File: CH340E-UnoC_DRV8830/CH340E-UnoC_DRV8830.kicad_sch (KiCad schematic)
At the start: 4 parts, among them J1 Power, J2 Digital/PWM, J3 Analog, J4 Digital/PWM

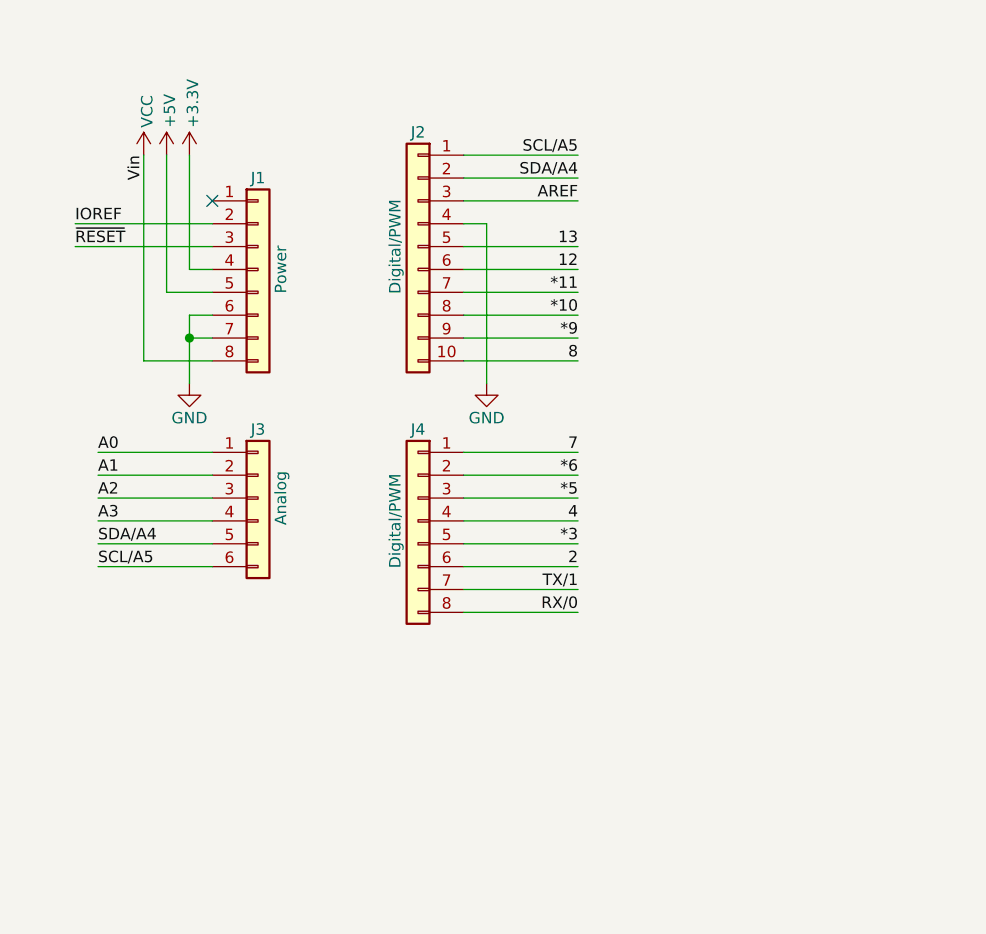
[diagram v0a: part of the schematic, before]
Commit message: feat: Atmega328P-PU was added to the schematic.
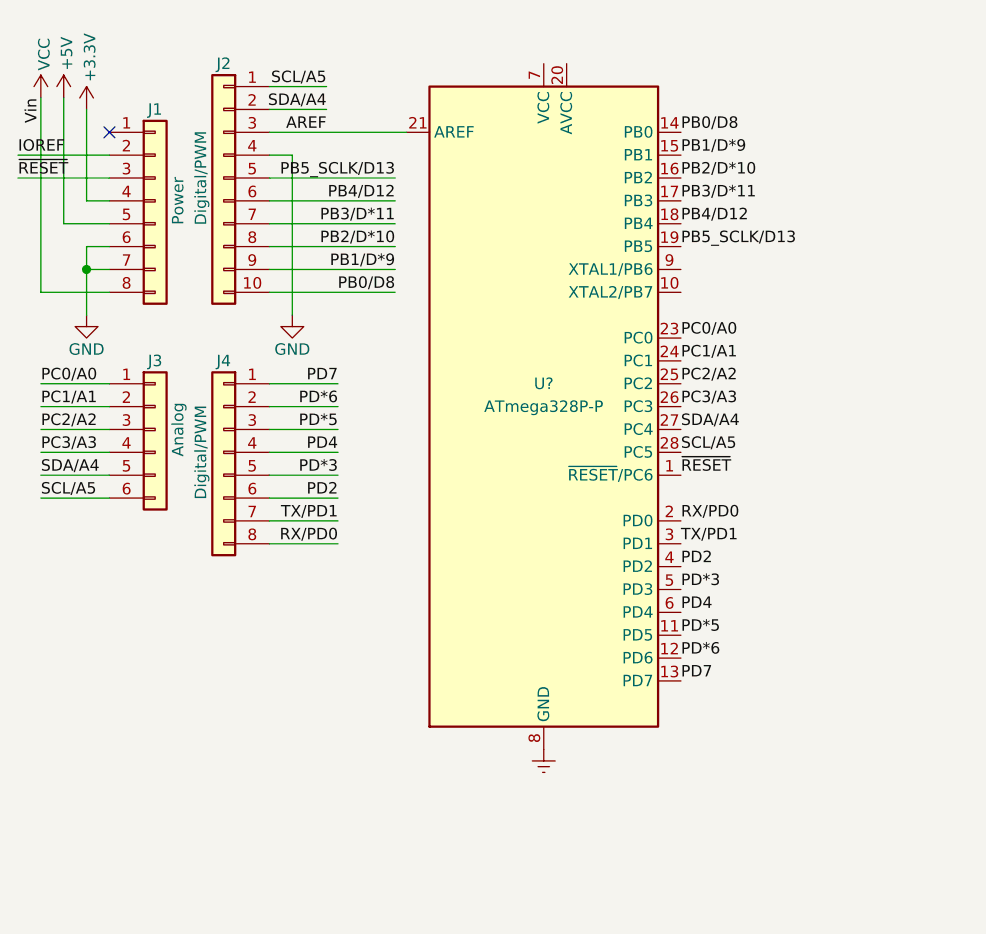
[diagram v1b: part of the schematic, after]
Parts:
- added U?: ATmega328P-P, Package_DIP:DIP-28_W7.62mm, symbol MCU_Microchip_ATmega:ATmega328P-P
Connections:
- net AREF: now also U?.21 (AREF)
- net SCL/A5: now also U?.28 (PC5)
- net SDA/A4: now also U?.27 (PC4)
- net ~{RESET}: now also U?.1 (~{RESET}/PC6)
- net *10 renamed PB2/D*10
- net PB2/D*10: now also U?.16 (PB2)
- net *11 renamed PB3/D*11
- net PB3/D*11: now also U?.17 (PB3)
- net *3 renamed PD*3
- net PD*3: now also U?.5 (PD3)
- net *5 renamed PD*5
- net PD*5: now also U?.11 (PD5)
- net *6 renamed PD*6
- net PD*6: now also U?.12 (PD6)
- net *9 renamed PB1/D*9
- net PB1/D*9: now also U?.15 (PB1)
- net 12 renamed PB4/D12
- net PB4/D12: now also U?.18 (PB4)
- net 13 renamed PB5_SCLK/D13
- net PB5_SCLK/D13: now also U?.19 (PB5)
- net 2 renamed PD2
- net PD2: now also U?.4 (PD2)
- net 4 renamed PD4
- net PD4: now also U?.6 (PD4)
- net 7 renamed PD7
- net PD7: now also U?.13 (PD7)
- net 8 renamed PB0/D8
- net PB0/D8: now also U?.14 (PB0)
- net A0 renamed PC0/A0
- net PC0/A0: now also U?.23 (PC0)
- net A1 renamed PC1/A1
- net PC1/A1: now also U?.24 (PC1)
- net A2 renamed PC2/A2
- net PC2/A2: now also U?.25 (PC2)
- net A3 renamed PC3/A3
- net PC3/A3: now also U?.26 (PC3)
- net RX/0 renamed RX/PD0
- net RX/PD0: now also U?.2 (PD0)
- net TX/1 renamed TX/PD1
- net TX/PD1: now also U?.3 (PD1)
- new net Earth: U?.22 (GND), U?.8 (GND)
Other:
- moved on the sheet: J1, J2, J3, J4

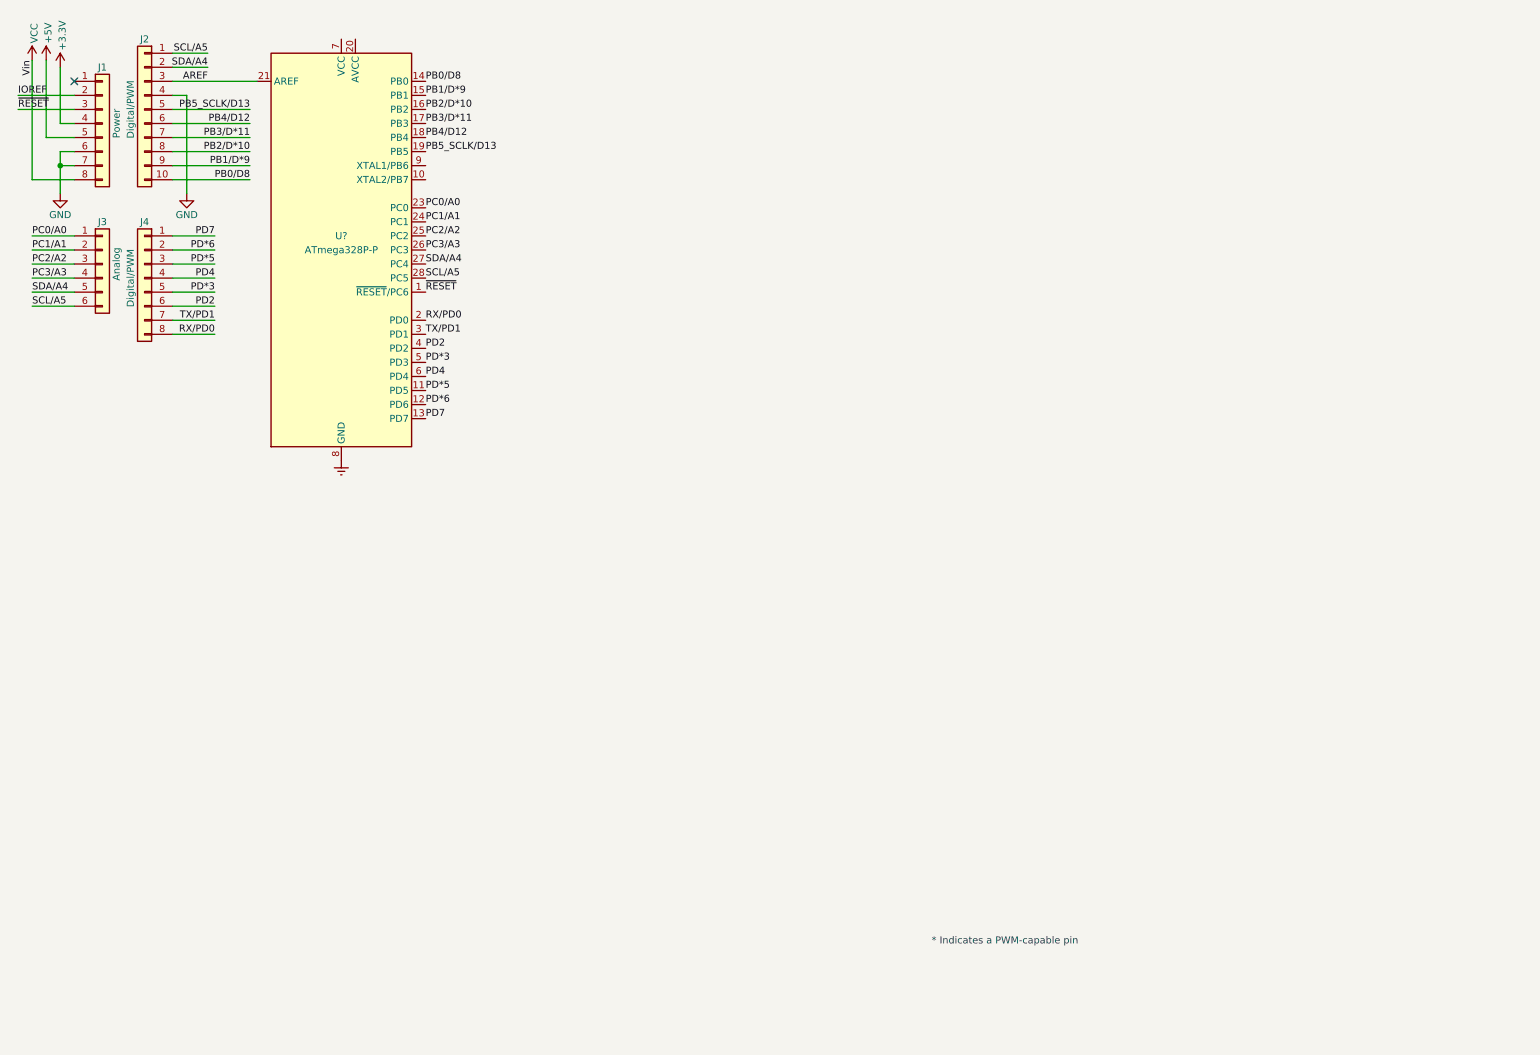
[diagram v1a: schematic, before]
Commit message: feat: Create Arduino Uno schematic using CH340E.
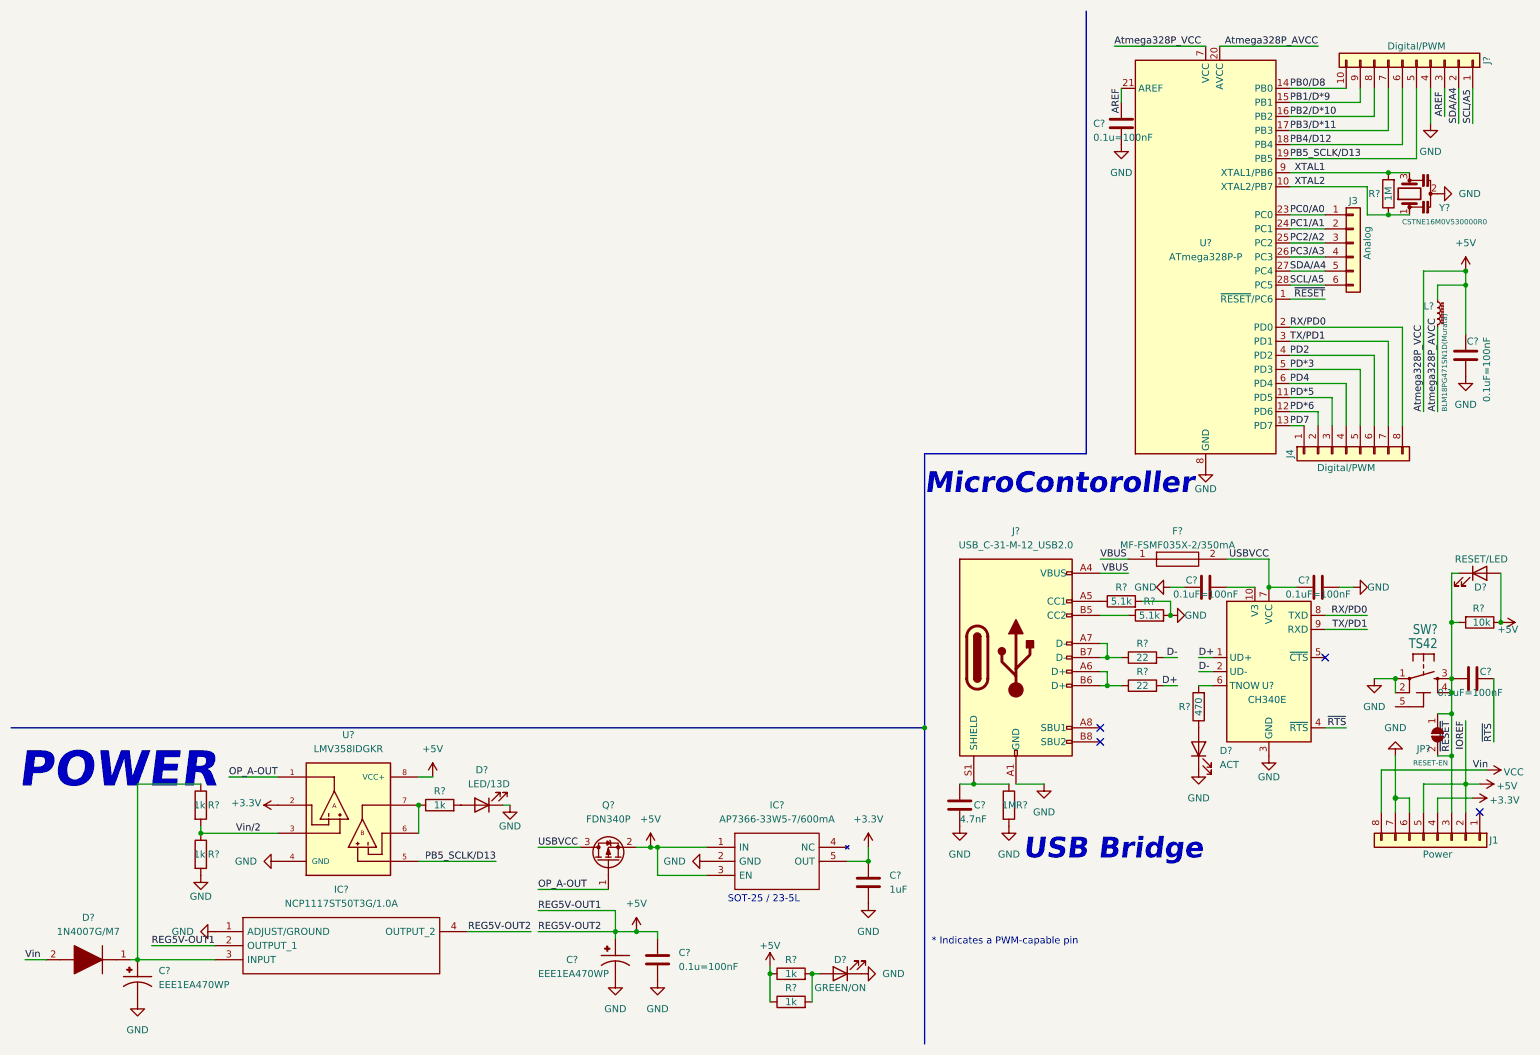
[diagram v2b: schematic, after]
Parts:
- removed J2: Digital/PWM, Connector_PinSocket_2.54mm:PinSocket_1x10_P2.54mm_Vertical, symbol Connector_Generic:Conn_01x10
- added C?: 1uF, symbol Device:C
- added C? (x2): 0.1u=100nF, symbol Device:C
- added C?: 4.7nF, symbol Device:C
- added C? (x2): EEE1EA470WP, CAP_EEE1EA470WP, symbol Capacitors-EEE1EA470WP_SnapEDA:EEE1EA470WP
- added C? (x4): 0.1uF=100nF, symbol Device:C
- added D?: ACT, symbol Device:LED
- added D?: GREEN/ON, symbol Device:LED
- added D?: RESET/LED, symbol Device:LED
- added D?: LED/13D, symbol Device:LED
- added D?: 1N4007G/M7, DIOM5025X220N, symbol Diode-1N4007G_SamacSys:1N4007G
- added F?: MF-FSMF035X-2/350mA, FUSC1608X65N, symbol Fuse_MF-FSMF035X-2_SamacSys:MF-FSMF035X-2
- added IC?: NCP1117ST50T3G/1.0A, SOT230P700X180-4N, symbol IC-Reg_NCP1117ST50T3G_SamacSys:NCP1117ST50T3G
- added IC?: AP7366-33W5-7/600mA, SOT95P285X130-5N, symbol IC-Reg_AP7366-33W5-7_SamacSys:AP7366-33W5-7
- added J?: Digital/PWM, Connector_PinSocket_2.54mm:PinSocket_1x10_P2.54mm_Vertical, symbol Connector_Generic:Conn_01x10
- added J?: USB_C-31-M-12_USB2.0, symbol Connector:USB_C_Receptacle_USB2.0
- added JP?: RESET-EN, symbol Jumper:SolderJumper_2_Open
- added L?: BLM18PG471SN1D(Murata), symbol Device:L_Ferrite_Small
- added Q?: FDN340P, Package_TO_SOT_SMD:SOT-23, symbol Transistor_FET:FDN340P
- added R?: 10k, symbol Device:R
- added R? (x2): 22, symbol Device:R
- added R? (x5): 1k, symbol Device:R
- added R?: 470, symbol Device:R
- added R? (x2): 1M, symbol Device:R
- added R? (x2): 5.1k, symbol Device:R
- added SW?: TS42, UNO-TH_Rev3e:TS42, symbol UNO-TH_Rev3e-eagle-import:TS42
- added U?: CH340E, Package_SO:MSOP-10_3x3mm_P0.5mm, symbol Interface_USB:CH340E
- added U?: LMV358IDGKR, SOP65P490X110-8N, symbol OPAmpDual_LMV358IDGKR_SnapEDA:LMV358IDGKR
- added Y?: CSTNE16M0V530000R0, symbol Device:Resonator
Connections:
- net Earth is gone; now on net GND: U?.22 (GND), U?.8 (GND)
- net IOREF is gone; now on net +5V: J1.2 (Pin_2)
- net +3V3: now also U?.2
- net +5V: now also U?.7 (VCC), C?.1, C?.1, C?.2, D?.2 (A), IC?.1 (IN), IC?.2 (OUTPUT_1), IC?.3 (EN), IC?.4 (OUTPUT_2), L?.1, Q?.2 (S), R?.1, R?.1, R?.1, U?.8 (VCC+)
- net AREF: now also C?.1, J?.3 (Pin_3)
- net GND: now also C?.1, C?.1, C?.2, C?.2, C?.2, C?.2, C?.2, C?.2, C?.2, D?.1 (K), D?.1 (K), D?.1 (K), IC?.1 (ADJUST/GROUND), IC?.2 (GND), J?.4 (Pin_4), J?.A1 (GND), J?.A12 (GND), J?.B1 (GND), J?.B12 (GND), R?.2, R?.2, R?.2, R?.2, SW?.1, SW?.2, U?.3 (GND), U?.4 (GND), Y?.2
- net PB0/D8: now also J?.10 (Pin_10)
- net PB1/D*9: now also J?.9 (Pin_9)
- net PB2/D*10: now also J?.8 (Pin_8)
- net PB3/D*11: now also J?.7 (Pin_7)
- net PB4/D12: now also J?.6 (Pin_6)
- net PB5_SCLK/D13: now also J?.5 (Pin_5), U?.5
- net RX/PD0: now also U?.8 (TXD)
- net SCL/A5: now also J?.1 (Pin_1)
- net SDA/A4: now also J?.2 (Pin_2)
- net TX/PD1: now also U?.9 (RXD)
- net VCC: now also D?.2
- net ~{RESET}: now also C?.2, D?.1 (K), JP?.1 (A), JP?.2 (B), R?.2, SW?.3, SW?.4
- net XTAL2: now reaches U?.10 (XTAL2/PB7)
- net XTAL2: now also R?.1, Y?.1
- net Atmega328P_AVCC: now reaches U?.20 (AVCC)
- net Atmega328P_AVCC: now also L?.2
- net XTAL1: now reaches U?.9 (XTAL1/PB6)
- net XTAL1: now also R?.2, Y?.3
- new net: C?.1, D?.1, IC?.3 (INPUT), R?.1
- new net: D?.2 (A), R?.1
- new net: D?.2 (A), R?.2, R?.2
- new net: C?.2, U?.10 (V3)
- new net: R?.2, U?.6 (TNOW)
- new net: J?.A6 (D+), J?.B6 (D+), R?.1
- new net: R?.1, U?.6, U?.7
- new net: D?.2 (A), R?.2
- new net: C?.1, J?.S1 (SHIELD), R?.1
- new net: J?.A7 (D-), J?.B7 (D-), R?.1
- new net: J?.A5 (CC1), R?.1
- new net: J?.B5 (CC2), R?.1
- new net +3.3V: C?.1, IC?.5 (OUT)
- new net D+: R?.2, U?.1 (UD+)
- new net D-: R?.2, U?.2 (UD-)
- new net OP_A-OUT: Q?.1 (G), U?.1
- new net USBVCC: C?.1, F?.2, Q?.3 (D), U?.7 (VCC)
- new net VBUS: F?.1, J?.A4 (VBUS), J?.A9 (VBUS), J?.B4 (VBUS), J?.B9 (VBUS)
- new net Vin/2: R?.1, R?.2, U?.3
- new net ~{RTS}: C?.1, U?.4 (~{RTS})
- no-connect marks 1 -> 4
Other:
- note added: "MicroContoroller"
- note added: "POWER"
- note added: "SOT-25 / 23-5L"
- note added: "USB Bridge"
- moved on the sheet: J1, J3, J4, U?

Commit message: feat: I have created a schematic of a motor driver using the DRV8830IC. A library of components has been added accordingly.
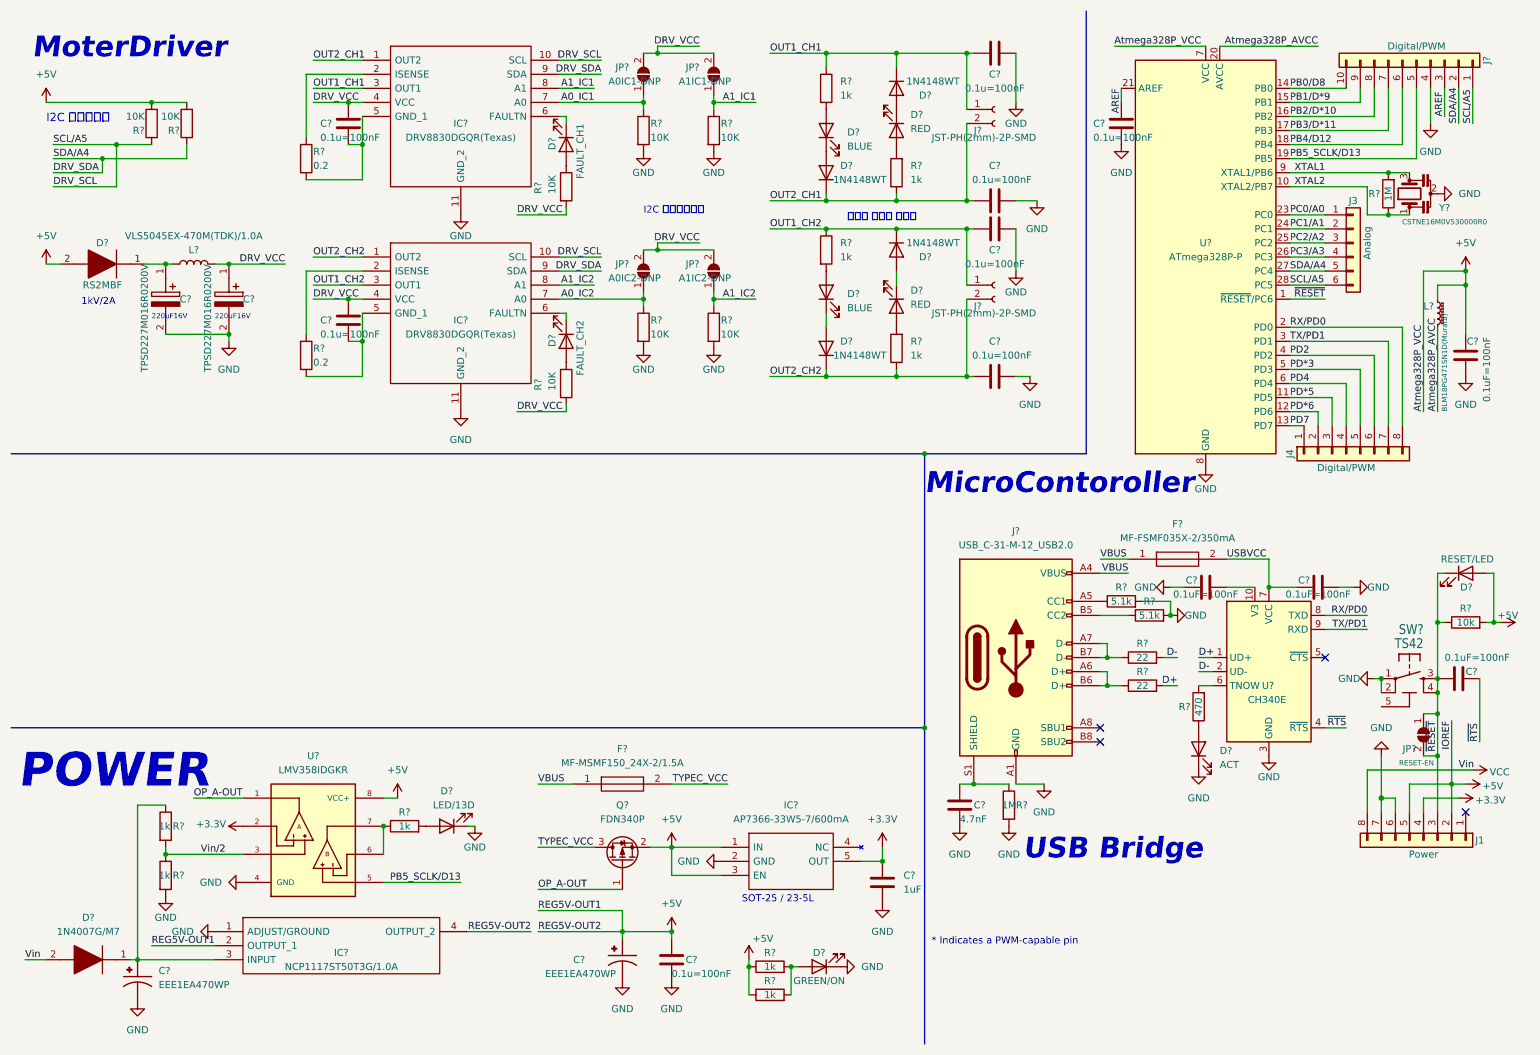
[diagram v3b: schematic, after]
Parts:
- removed R?: 10k, symbol Device:R
- added C? (x2): TPSD227M016R0200V, CAPPM7344X310N, symbol Cap220uF16V_TPSD227M016R0200V_SamacSys:TPSD227M016R0200V
- added C? (x6): 0.1u=100nF, Capacitor_SMD:C_0402_1005Metric, symbol Device:C
- added D? (x4): 1N4148WT, Diode_SMD:D_SOD-523, symbol Diode:1N4148WT
- added D? (x2): BLUE, LED_SMD:LED_0402_1005Metric, symbol Device:LED
- added D?: FAULT_CH2, LED_SMD:LED_0402_1005Metric, symbol Device:LED
- added D? (x2): RED, LED_SMD:LED_0402_1005Metric, symbol Device:LED
- added D?: RS2MBF, SODFL5336X130N, symbol Diodes1kV2A_RS2MBF_SMD_SamacSys:RS2MBF
- added D?: FAULT_CH1, LED_SMD:LED_0402_1005Metric, symbol Device:LED
- added F?: MF-MSMF150_24X-2/1.5A, FUSC4632X160N, symbol Fuse_MF-MSMF150_24X-2_1812 (4532 Metric)_SamacSys:MF-MSMF150_24X-2
- added IC? (x2): DRV8830DGQR(Texas), SOP50P490X110-11N, symbol IC-DRV8830DGQR_SamacSys:DRV8830DGQR
- added J? (x2): JST-PH(2mm)-2P-SMD, Connector_JST:JST_PH_B2B-PH-SM4-TB_1x02-1MP_P2.00mm_Vertical, symbol Connector:Conn_01x02_Female
- added JP?: A1IC2-DNP, symbol Jumper:SolderJumper_2_Open
- added JP?: A0IC1-DNP, symbol Jumper:SolderJumper_2_Open
- added JP?: A0IC2-DNP, symbol Jumper:SolderJumper_2_Open
- added JP?: A1IC1-DNP, symbol Jumper:SolderJumper_2_Open
- added L?: VLS5045EX-470M(TDK)/1.0A, symbol Device:L
- added R? (x4): 1k, Resistor_SMD:R_0402_1005Metric, symbol Device:R
- added R? (x8): 10K, Resistor_SMD:R_0402_1005Metric, symbol Device:R
- added R?: 10k, symbol Device:R
- added R? (x2): 0.2, Resistor_SMD:R_0402_1005Metric, symbol Device:R
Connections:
- net +5V: now also D?.2, R?.2, R?.2, R?.2
- net GND: now also C?.2, C?.2, C?.2, C?.2, C?.2, C?.2, IC?.11 (GND_2), IC?.11 (GND_2), R?.2, R?.2, R?.2, R?.2
- net USBVCC: no longer Q?.3 (D)
- net VBUS: now also F?.1
- net ~{RESET}: now also R?.1
- net SCL/A5 renamed DRV_SCL
- net DRV_SCL: now also IC?.10 (SCL), IC?.10 (SCL), R?.1
- net SDA/A4 renamed DRV_SDA
- net DRV_SDA: now also IC?.9 (SDA), IC?.9 (SDA), R?.1
- new net: D?.1 (K), D?.2 (A) (x4)
- new net: D?.2 (A), R?.2 (x4)
- new net: D?.2 (A), R?.1 (x2)
- new net: C?.1, D?.1, L?.1
- new net: IC?.2 (ISENSE), R?.1 (x2)
- new net: C?.2, IC?.5 (GND_1), R?.2 (x2)
- new net: D?.1 (K), IC?.6 (FAULTN) (x2)
- new net A0_IC1: IC?.7 (A0), JP?.1 (A), R?.1
- new net A0_IC2: IC?.7 (A0), JP?.1 (A), R?.1
- new net A1_IC1: IC?.8 (A1), JP?.1 (A), R?.1
- new net A1_IC2: IC?.8 (A1), JP?.1 (A), R?.1
- new net DRV_VCC: C?.1, C?.1, C?.1, IC?.4 (VCC), IC?.4 (VCC), JP?.2 (B), JP?.2 (B), JP?.2 (B), JP?.2 (B), L?.2, R?.2, R?.2
- new net OUT1_CH1: C?.1, D?.1 (K), IC?.3 (OUT1), J?.1 (Pin_1), R?.1
- new net OUT1_CH2: C?.1, D?.1 (K), IC?.3 (OUT1), J?.1 (Pin_1), R?.1
- new net OUT2_CH1: C?.1, D?.1 (K), IC?.1 (OUT2), J?.2 (Pin_2), R?.1
- new net OUT2_CH2: C?.1, D?.1 (K), IC?.1 (OUT2), J?.2 (Pin_2), R?.1
- new net TYPEC_VCC: F?.2, Q?.3 (D)
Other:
- note added: "1kV/2A"
- note added: "220uF16V"
- note added: "I2C アドレス設定"
- note added: "I2C プルアップ"
- note added: "MoterDriver"
- note added: "モータ 正転青 逆転赤"
- moved on the sheet: C?, D?, IC?, J1, JP?, Q?, R?, SW?, U?
